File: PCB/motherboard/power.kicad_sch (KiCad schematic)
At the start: 28 parts, among them U1 TPS54140ADGQR, U2 PTPS259830LNRGER, U3 AP2112K-3.3TRG1

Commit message: test kicad collab
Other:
- moved on the sheet: C1, R6
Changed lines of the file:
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@@
 		)
 	)
+	(text_box "dA cAPIRE TENSIONE USCITA ANALOG \n"
+		(exclude_from_sim no)
+		(at 260.35 27.94 0)
+		(size 22.86 10.795)
+		(margins 0.9525 0.9525 0.9525 0.9525)
+		(stroke
+			(width 0)
+			(type solid)
+		)
+		(fill
+			(type none)
+		)
+		(effects
+			(font
+				(size 1.27 1.27)
+			)
+			(justify left top)
+		)
+	)
+	(text_box "LED POWER STATUS\n"
+		(exclude_from_sim no)
+		(at 259.715 53.975 0)
+		(size 21.59 8.89)
+		(margins 0.9525 0.9525 0.9525 0.9525)
+		(stroke
+			(width 0)
+			(type solid)
+		)
+		(fill
+			(type none)
+		)
+		(effects
+			(font
+				(size 1.27 1.27)
+			)
+			(justify left top)
+		)
+	)
 	(text_box "Da settare tutti i valori di strapping resistenze e cap\n"
 		(exclude_from_sim no)
@@
 		)
 	)
+	(text_box "Capire a cosa serve il diodo da datasheet"
+		(exclude_from_sim no)
+		(at 130.175 118.745 0)
+		(size 22.225 10.795)
+		(margins 0.9525 0.9525 0.9525 0.9525)
+		(stroke
+			(width 0)
+			(type solid)
+		)
+		(fill
+			(type none)
+		)
+		(effects
+			(font
+				(size 1.27 1.27)
+			)
+			(justify left top)
+		)
+	)
 	(junction
 		(at 130.81 147.32)
@@
 	)
 	(junction
+		(at 104.14 60.96)
+		(diameter 0)
+		(color 0 0 0 0)
+	)
+	(junction
 		(at 22.86 149.86)
 		(diameter 0)
@@
 	(wire
 		(pts
+			(xy 104.14 60.96) (xy 104.14 62.23)
+		)
+		(stroke
+			(width 0)
+			(type default)
+		)
+	)
+	(wire
+		(pts
 			(xy 62.23 27.94) (xy 62.23 40.64)
 		)
@@
 	(wire
 		(pts
-			(xy 104.14 60.96) (xy 132.08 60.96)
+			(xy 101.6 60.96) (xy 104.14 60.96)
 		)
 		(stroke
@@
 	(wire
 		(pts
-			(xy 87.63 55.88) (xy 132.08 55.88)
+			(xy 83.82 55.88) (xy 132.08 55.88)
 		)
 		(stroke
@@
 	(wire
 		(pts
-			(xy 92.71 58.42) (xy 132.08 58.42)
+			(xy 90.17 58.42) (xy 132.08 58.42)
 		)
 		(stroke
@@
 	(wire
 		(pts
-			(xy 104.14 62.23) (xy 104.14 60.96)
-		)
-		(stroke
-			(width 0)
-			(type default)
-		)
-	)
-	(wire
-		(pts
 			(xy 44.45 130.81) (xy 44.45 147.32)
 		)
@@
 	(wire
 		(pts
-			(xy 92.71 67.31) (xy 92.71 68.58)
+			(xy 90.17 67.31) (xy 90.17 68.58)
 		)
 		(stroke
@@
 	(wire
 		(pts
+			(xy 104.14 60.96) (xy 132.08 60.96)
+		)
+		(stroke
+			(width 0)
+			(type default)
+		)
+	)
+	(wire
+		(pts
 			(xy 43.18 157.48) (xy 45.72 157.48)
 		)
@@
 	(wire
 		(pts
-			(xy 87.63 67.31) (xy 87.63 68.58)
+			(xy 83.82 67.31) (xy 83.82 68.58)
 		)
 		(stroke
@@
 	(wire
 		(pts
-			(xy 92.71 59.69) (xy 92.71 58.42)
+			(xy 90.17 59.69) (xy 90.17 58.42)
 		)
 		(stroke
@@
 	(wire
 		(pts
-			(xy 87.63 59.69) (xy 87.63 55.88)
+			(xy 83.82 59.69) (xy 83.82 55.88)
 		)
 		(stroke
@@
 	(hierarchical_label "IMON"
 		(shape input)
-		(at 104.14 60.96 180)
+		(at 101.6 60.96 180)
 		(effects
 			(font
@@
 	(symbol
 		(lib_id "power:GND")
-		(at 92.71 68.58 0)
+		(at 90.17 68.58 0)
 		(unit 1)
 		(exclude_from_sim no)
@@
 		(fields_autoplaced yes)
 		(property "Reference" "#PWR017"
-			(at 92.71 74.93 0)
+			(at 90.17 74.93 0)
 			(effects
 				(font
@@
 		)
 		(property "Value" "GND"
-			(at 92.71 73.66 0)
+			(at 90.17 73.66 0)
 			(effects
 				(font
@@
 		)
 		(property "Footprint" ""
-			(at 92.71 68.58 0)
+			(at 90.17 68.58 0)
 			(effects
 				(font
@@
 		)
 		(property "Datasheet" ""
-			(at 92.71 68.58 0)
+			(at 90.17 68.58 0)
 			(effects
 				(font
@@
 		)
 		(property "Description" "Power symbol creates a global label with name \"GND\" , ground"
-			(at 92.71 68.58 0)
+			(at 90.17 68.58 0)
 			(effects
 				(font
@@
 	(symbol
 		(lib_id "power:GND")
-		(at 87.63 68.58 0)
+		(at 83.82 68.58 0)
 		(unit 1)
 		(exclude_from_sim no)
@@
 		(fields_autoplaced yes)
 		(property "Reference" "#PWR09"
-			(at 87.63 74.93 0)
+			(at 83.82 74.93 0)
 			(effects
 				(font
@@
 		)
 		(property "Value" "GND"
-			(at 87.63 73.66 0)
+			(at 83.82 73.66 0)
 			(effects
 				(font
@@
 		)
 		(property "Footprint" ""
-			(at 87.63 68.58 0)
+			(at 83.82 68.58 0)
 			(effects
 				(font
@@
 		)
 		(property "Datasheet" ""
-			(at 87.63 68.58 0)
+			(at 83.82 68.58 0)
 			(effects
 				(font
@@
 		)
 		(property "Description" "Power symbol creates a global label with name \"GND\" , ground"
-			(at 87.63 68.58 0)
+			(at 83.82 68.58 0)
 			(effects
 				(font
@@
 	(symbol
 		(lib_id "Device:C")
-		(at 87.63 63.5 0)
+		(at 83.82 63.5 0)
 		(unit 1)
 		(exclude_from_sim no)
@@
 		(dnp no)
 		(property "Reference" "C1"
-			(at 83.566 61.468 0)
+			(at 79.756 61.214 0)
 			(effects
 				(font
@@
 		)
 		(property "Value" "C"
-			(at 83.82 64.008 0)
+			(at 79.756 64.516 0)
 			(effects
 				(font
@@
 		)
 		(property "Footprint" ""
-			(at 88.5952 67.31 0)
+			(at 84.7852 67.31 0)
 			(effects
 				(font
@@
 		)
 		(property "Datasheet" "~"
-			(at 87.63 63.5 0)
+			(at 83.82 63.5 0)
 			(effects
 				(font
@@
 		)
 		(property "Description" "Unpolarized capacitor"
-			(at 87.63 63.5 0)
+			(at 83.82 63.5 0)
 			(effects
 				(font
@@
 	(symbol
 		(lib_id "Device:R")
-		(at 92.71 63.5 0)
+		(at 90.17 63.5 0)
 		(unit 1)
 		(exclude_from_sim no)
@@
 		(on_board yes)
 		(dnp no)
-		(fields_autoplaced yes)
 		(property "Reference" "R6"
-			(at 95.25 62.2299 0)
+			(at 91.694 62.23 0)
 			(effects
 				(font
@@
 		)
 		(property "Value" "R"
-			(at 95.25 64.7699 0)
+			(at 92.202 64.516 0)
 			(effects
 				(font
@@
 		)
 		(property "Footprint" ""
-			(at 90.932 63.5 90)
+			(at 88.392 63.5 90)
 			(effects
 				(font
@@
 		)
 		(property "Datasheet" "~"
-			(at 92.71 63.5 0)
+			(at 90.17 63.5 0)
 			(effects
 				(font
@@
 		)
 		(property "Description" "Resistor"
-			(at 92.71 63.5 0)
+			(at 90.17 63.5 0)
 			(effects
 				(font
@@
 		(on_board yes)
 		(dnp no)
-		(fields_autoplaced yes)
 		(property "Reference" "R3"
-			(at 78.74 62.2299 0)
+			(at 72.136 61.976 0)
 			(effects
 				(font
@@
 		)
 		(property "Value" "R"
-			(at 78.74 64.7699 0)
+			(at 73.152 64.516 0)
 			(effects
 				(font

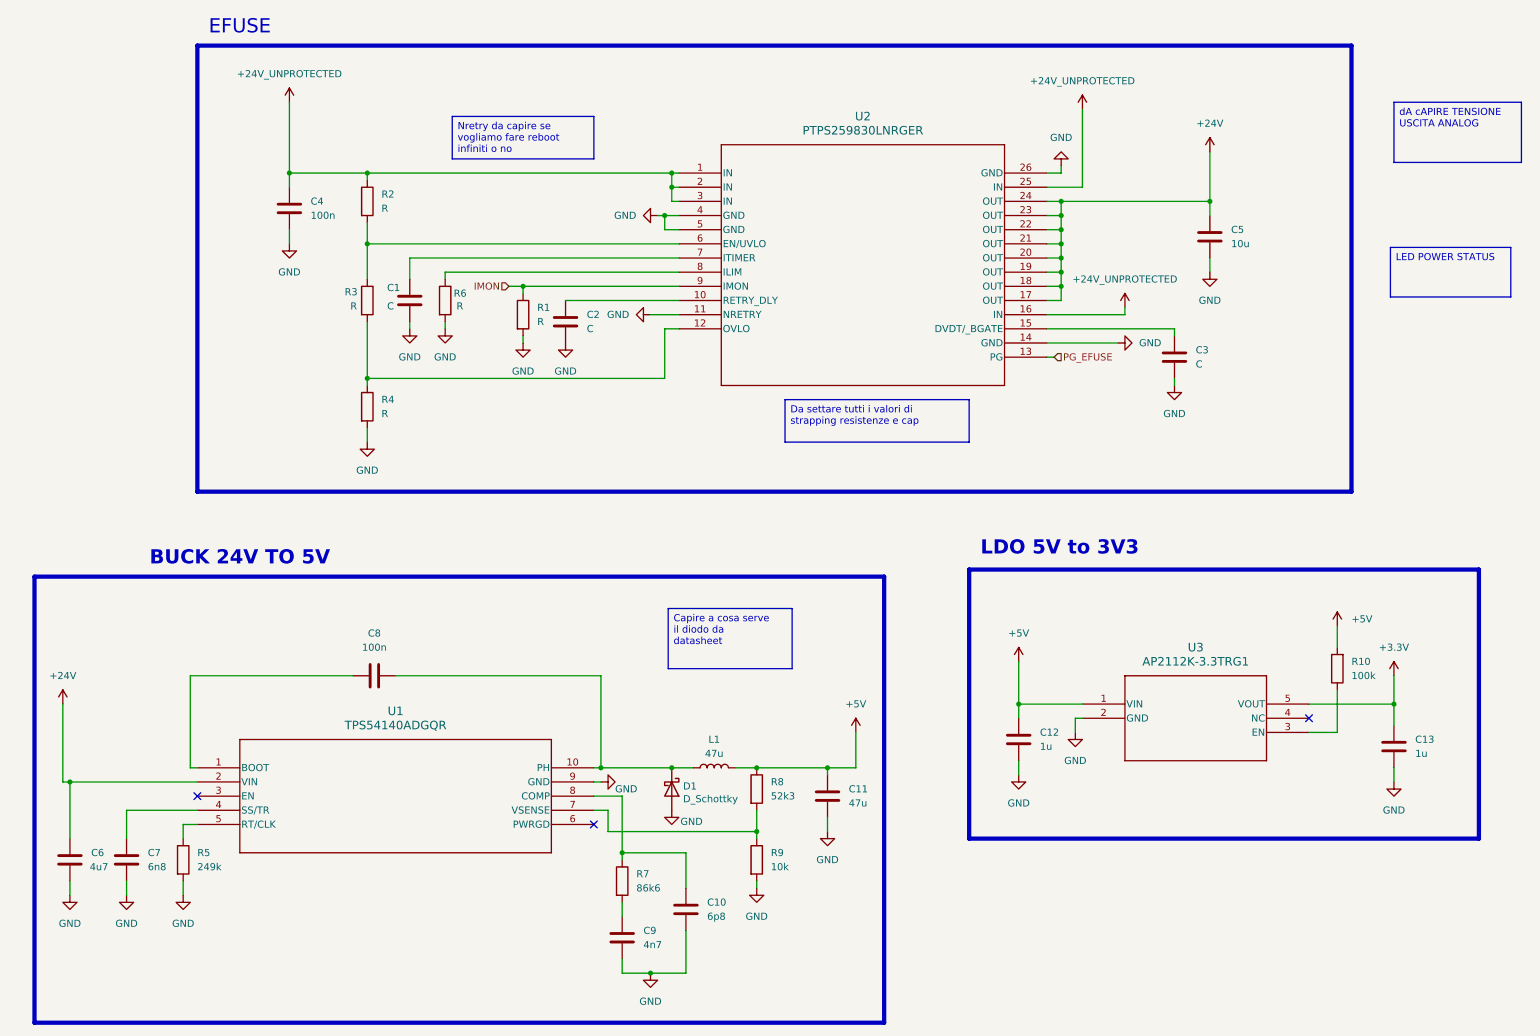
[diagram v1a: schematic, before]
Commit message: reverse current protection on ESCON+others
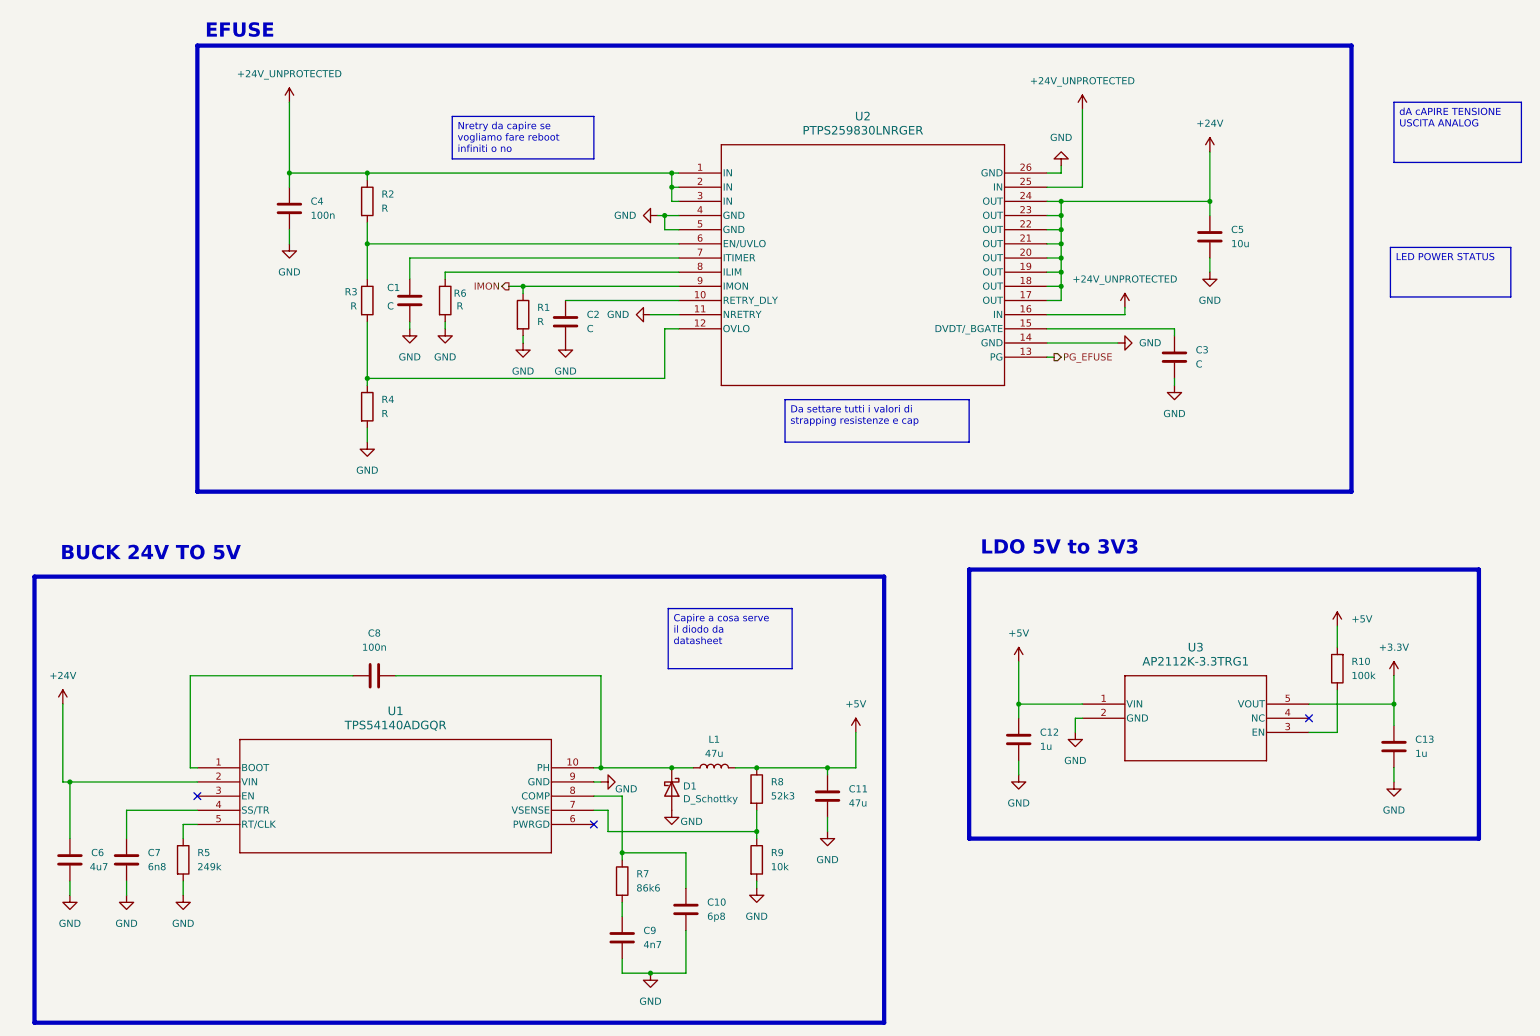
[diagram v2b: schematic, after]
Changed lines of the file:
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@@
 	(text "BUCK 24V TO 5V"
 		(exclude_from_sim no)
-		(at 53.34 109.728 0)
+		(at 37.338 108.966 0)
 		(effects
 			(font
-				(face "Arkhip")
 				(size 2.54 2.54)
 				(bold yes)
@@
 		(effects
 			(font
-				(face "Arkhip")
 				(size 2.54 2.54)
 				(bold yes)
@@
 	(text "EFUSE\n"
 		(exclude_from_sim no)
-		(at 53.34 14.478 0)
+		(at 53.34 15.24 0)
 		(effects
 			(font
-				(face "Arkhip")
 				(size 2.54 2.54)
+				(thickness 0.508)
+				(bold yes)
 			)
 		)
@@
 	)
 	(hierarchical_label "IMON"
-		(shape input)
+		(shape output)
 		(at 101.6 60.96 180)
 		(effects
@@
 	)
 	(hierarchical_label "PG_EFUSE"
-		(shape input)
+		(shape output)
 		(at 199.39 73.66 0)
 		(effects

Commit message: collegamenti tra blocchi schematico, sistemati connettori,finita la parte di shunt monitor per back EMF escon, aggiunti status LED, aggiunti bulk cap su alimentazione+altre modifiche
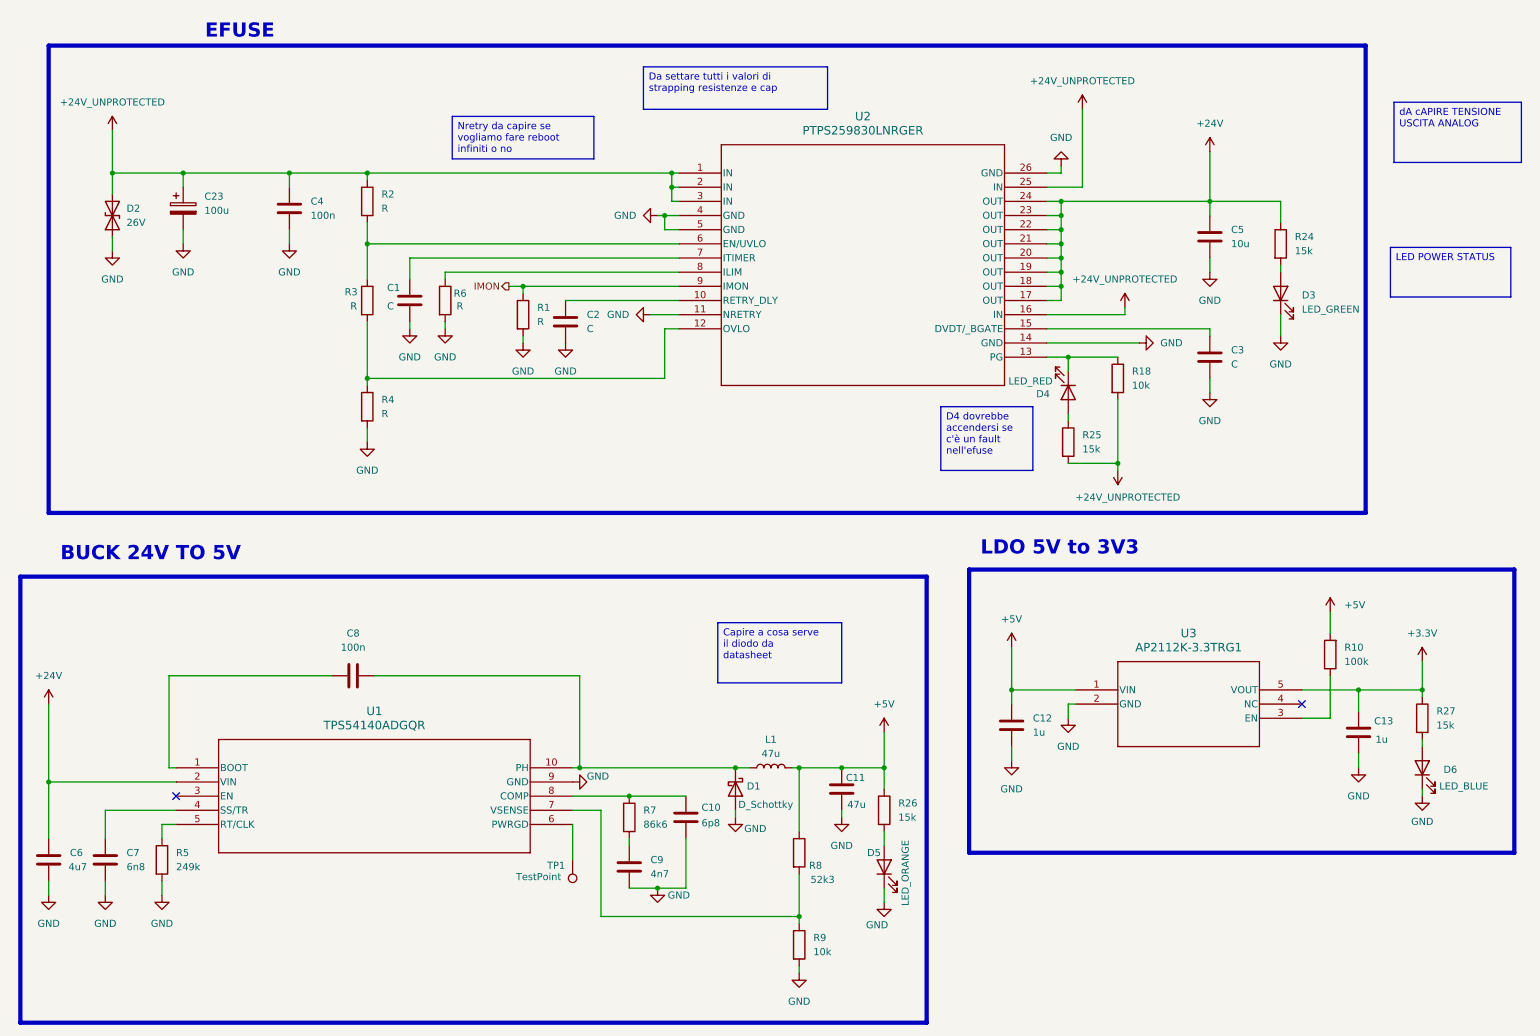
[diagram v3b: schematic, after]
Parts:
- added C23: 100u, symbol Device:C_Polarized
- added D2: 26V, symbol Device:D_TVS
- added D3: LED_GREEN, symbol Device:LED
- added D4: LED_RED, symbol Device:LED
- added D5: LED_ORANGE, symbol Device:LED
- added D6: LED_BLUE, symbol Device:LED
- added R18: 10k, symbol Device:R
- added R24, R25, R26, R27: 15k, symbol Device:R
- added TP1: TestPoint, symbol Connector:TestPoint
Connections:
- net +24V: now also R24.1
- net +24V_UNPROTECTED: now also C23.1, D2.2 (A2), R18.2, R25.2
- net +3.3V: now also R27.1
- net +5V: now also R26.1
- net GND: now also C23.2, D2.1 (A1), D3.1 (K), D5.1 (K), D6.1 (K)
- net at U1.6 (PWRGD): now also TP1.1
- net PG_EFUSE: no longer names the net of U2.13 (PG)
- net PG_EFUSE: now also D4.1 (K), R18.1
- new net: D6.2 (A), R27.2
- new net: D4.2 (A), R25.1
- new net: D5.2 (A), R26.2
- new net: D3.2 (A), R24.2
- no-connect marks 3 -> 2
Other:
- moved on the sheet: C10, C11, C12, C13, C3, C6, C7, C8, C9, D1, L1, R10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
